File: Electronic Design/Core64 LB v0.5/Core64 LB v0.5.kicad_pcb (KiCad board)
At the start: 2 copper layers, 85 x 170 mm, 146 parts, among them IC1 TPS7A0533PDBVR, IC2 LP3961EMP-5.0, IC3 NCP176AMX330TCG, J1 HEADER_8-PIN_0.1, J10 TSM-106-03-T-DV‎, J11 SSW-116-22-F-S-VS‎, J12 TEENSY Cur. Mon., J13 Core Cur. Mon., J14 SSW-116-22-F-S-VS‎, J17 LED Cur. Mon., J2 HEADER_11-PIN_0.1, J3 Conn_01x08_Female, J4 PRG, J5 HEADER_8-PIN_0.1, J6 HEADER_8-PIN_0.1, J7 S03B-PASK-2_LF__SN_, J8 5V0 Cur. Mon., J9 3V3 Cur. Mon., Q1 MCC_SL3401A, Q10 MMBT4403LT1G, Q11 MMBT4403LT1G, Q12 MMBT4401LT1G, Q13 MMBT4403LT1G, Q14 MMBT4403LT1G, Q15 MMBT4401LT1G, Q16 MMBT4403LT1G, Q17 MMBT4403LT1G, Q18 MMBT4401LT1G, Q19 MMBT4401LT1G, Q2 MMBT4403LT1G, Q20 MMBT4401LT1G, Q21 MMBT4401LT1G, Q22 Q_NMOS_DGS_NVTR4503NT1G, Q3 MMBT4403LT1G, Q4 MMBT4403LT1G, Q5 MMBT4403LT1G, Q6 MMBT4401LT1G, Q7 MMBT4401LT1G, Q8 MMBT4401LT1G, Q9 MMBT4401LT1G, SW1 JS102011SAQN, U1 74HC02, U2 Teensy3.2, U3 SN74LV1T125DBVR, U4 M24C01-RMN, U5 74HC238, U6 Micro_LiPo_Charger, U7 LM393, U8 Adafruit_3.2_TFT_1743, X1 QWIIC, X2 Header_9-PIN_0.1, X3 SAO_conn_SFH11-NBPC-D03-ST-BK, X4 SSW-104-22-L-S-VS

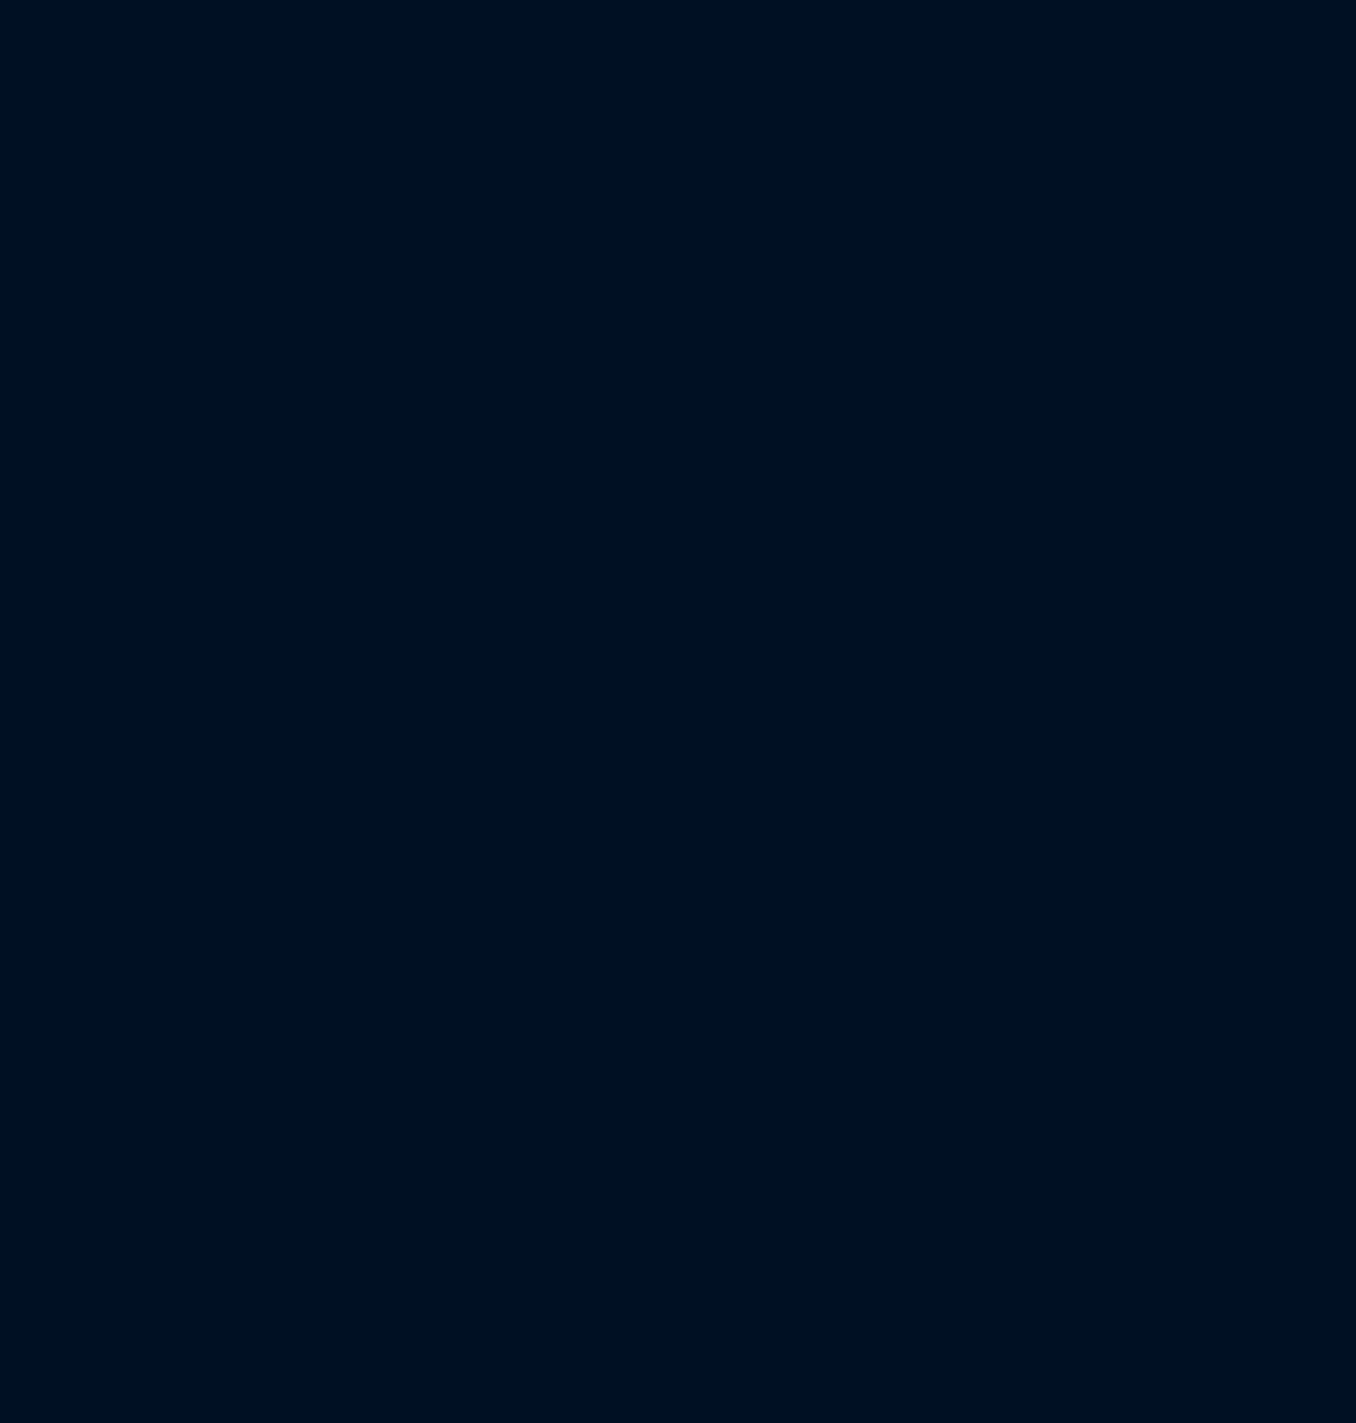
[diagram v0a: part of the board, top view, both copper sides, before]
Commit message: Update CB to be compatible with LM V0.1
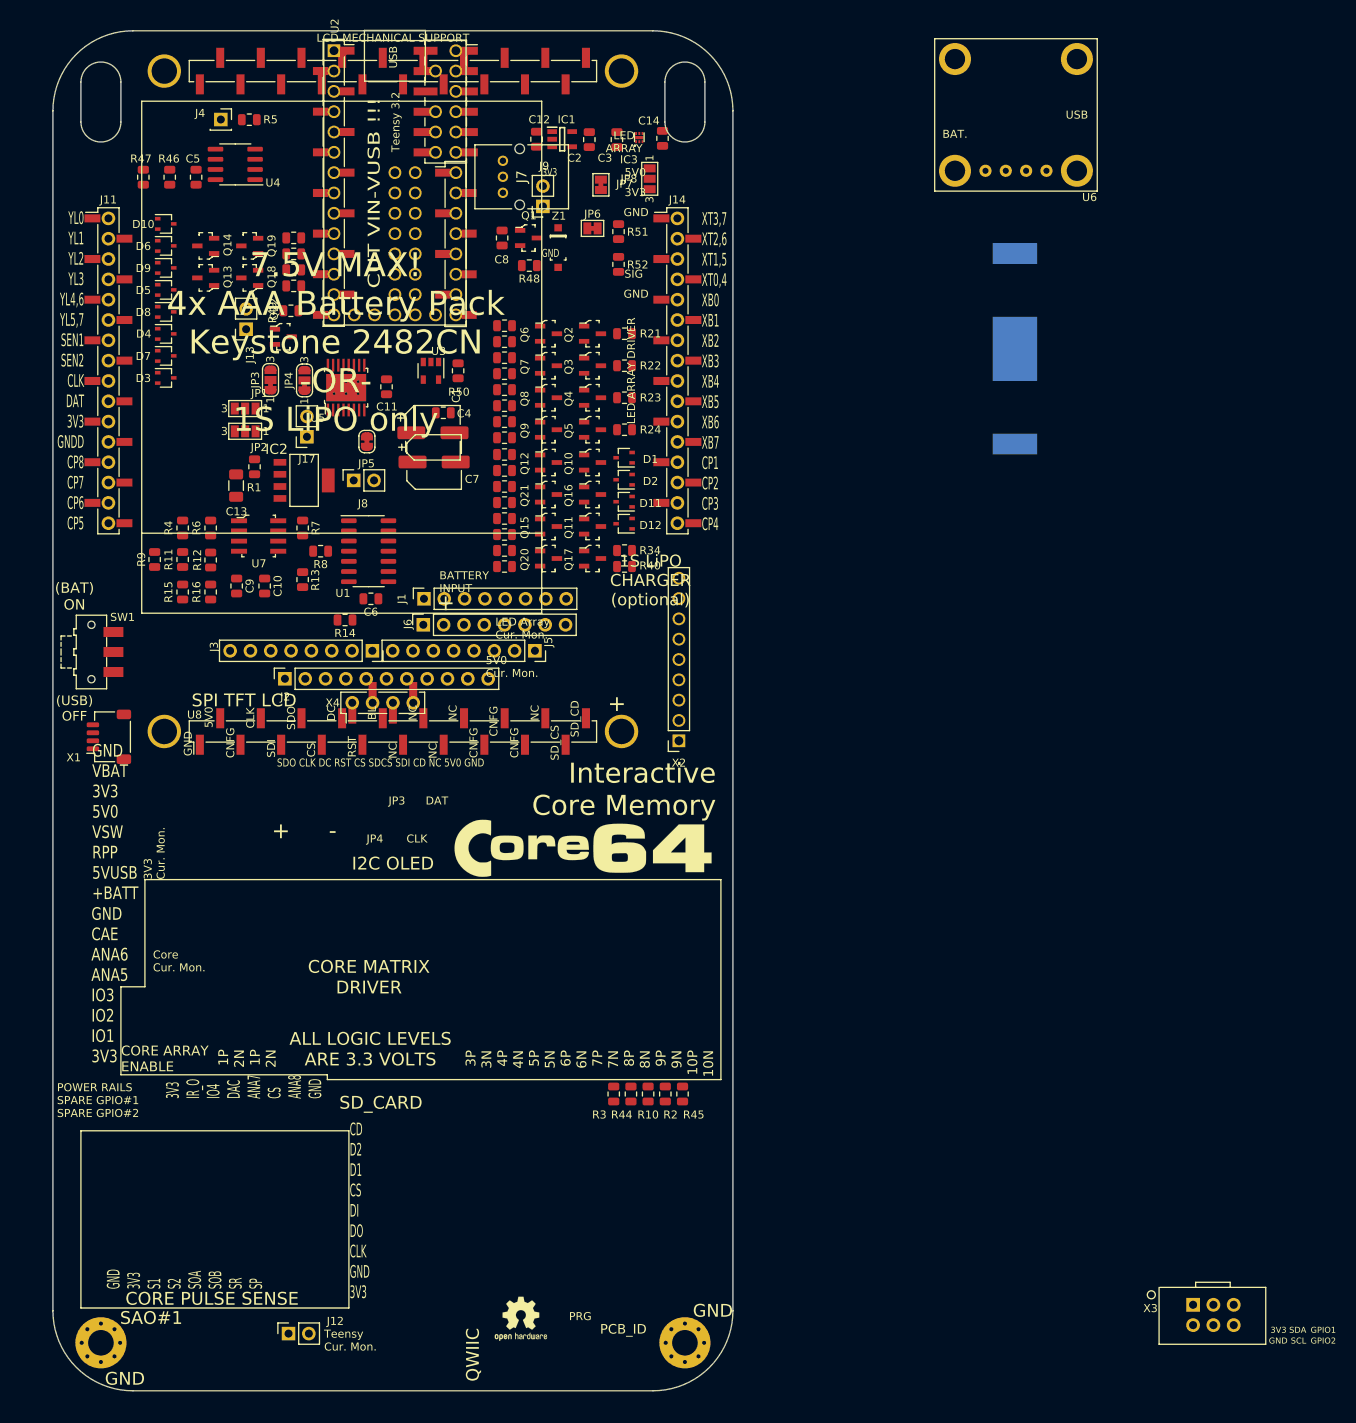
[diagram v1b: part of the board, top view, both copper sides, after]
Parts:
- added BT1: 3V, Battery:BatteryHolder_MPD_BC2003_1x2032, B.Cu at (229.2, -4.50)
- added C1: 470uF, Capacitor_SMD:CP_Elec_6.3x7.7, F.Cu at (156.5, 6.00)
- added C10: 10uF, Capacitor_SMD:C_0805_2012Metric, F.Cu at (135.5, 25.1)
- added C11: 0.1uF, Capacitor_SMD:C_0805_2012Metric, F.Cu at (150.7, 0.25)
- added C12: 1uF, Capacitor_SMD:C_0805_2012Metric, F.Cu at (169.4, -30.7)
- added C13: 68uF, Capacitor_SMD:C_1206_3216Metric, F.Cu at (131.9, 12.6)
- added C14: 1uF, Capacitor_SMD:C_0805_2012Metric, F.Cu at (185.2, -30.8)
- added C2: 1uF, Capacitor_SMD:C_0805_2012Metric, F.Cu at (176.1, -30.6)
- added C3: 1uF, Capacitor_SMD:C_0805_2012Metric, F.Cu at (179.5, -30.6)
- added C4: 0.1uF, Capacitor_SMD:C_0805_2012Metric, F.Cu at (157.8, 3.50)
- added C5: 0.1uF, Capacitor_SMD:C_0805_2012Metric, F.Cu at (126.9, -25.9)
- added C6: 0.1uF, Capacitor_SMD:C_0805_2012Metric, F.Cu at (148.8, 26.8)
- added C7: 470uF, Capacitor_SMD:CP_Elec_6.3x7.7, F.Cu at (156.7, 9.65)
- added C8: 0.01uF, Capacitor_SMD:C_0805_2012Metric, F.Cu at (165.2, -18.4)
- added C9: 0.1uF, Capacitor_SMD:C_0805_2012Metric, F.Cu at (132.0, 25.1)
- added D1: BAT54AW, Package_TO_SOT_SMD:SOT-323_SC-70, F.Cu at (180.4, 9.12)
- added D10: BAT54CW, Package_TO_SOT_SMD:SOT-323_SC-70, F.Cu at (123.1, -20.1)
- added D11: BAT54AW, Package_TO_SOT_SMD:SOT-323_SC-70, F.Cu at (180.4, 14.6)
- added D12: BAT54CW, Package_TO_SOT_SMD:SOT-323_SC-70, F.Cu at (180.4, 17.4)
- added D2: BAT54CW, Package_TO_SOT_SMD:SOT-323_SC-70, F.Cu at (180.4, 11.9)
- added D3: BAT54AW, Package_TO_SOT_SMD:SOT-323_SC-70, F.Cu at (123.1, -0.86)
- added D4: BAT54AW, Package_TO_SOT_SMD:SOT-323_SC-70, F.Cu at (123.1, -6.37)
- added D5: BAT54AW, Package_TO_SOT_SMD:SOT-323_SC-70, F.Cu at (123.1, -11.9)
- added D6: BAT54AW, Package_TO_SOT_SMD:SOT-323_SC-70, F.Cu at (123.1, -17.4)
- added D7: BAT54CW, Package_TO_SOT_SMD:SOT-323_SC-70, F.Cu at (123.1, -3.62)
- added D8: BAT54CW, Package_TO_SOT_SMD:SOT-323_SC-70, F.Cu at (123.1, -9.12)
- added D9: BAT54CW, Package_TO_SOT_SMD:SOT-323_SC-70, F.Cu at (123.1, -14.6)
- added H1: GND PAD, MountingHole:MountingHole_3.2mm_M3_Pad_Via, F.Cu at (115.0, 119.8)
- added H2: GND PAD, MountingHole:MountingHole_3.2mm_M3_Pad_Via, F.Cu at (188.0, 119.8)
- added IC1: TPS7A0533PDBVR, TPS7A0533PDBVR:SOT95P280X145-5N, F.Cu at (172.7, -30.7)
- added IC2: LP3961EMP-5.0, LP3961EMP-5.0:SOT150P696X180-5N, F.Cu at (140.4, 11.9)
- added IC3: NCP176AMX330TCG, NCP176AMX330TCG:NCP176AMX330TCG, F.Cu at (182.3, -30.9)
- added J1: HEADER_8-PIN_0.1, Connector_PinSocket_2.54mm:PinSocket_1x08_P2.54mm_Vertical, F.Cu at (155.4, 26.8)
- added J11: SSW-116-22-F-S-VS‎, Connector_PinHeader_2.54mm:PinHeader_1x16_P2.54mm_Vertical_SMD_and_TH_Pin1Left, F.Cu at (115.9, -1.75)
- added J12: TEENSY Cur. Mon., Connector_PinSocket_2.54mm:PinSocket_1x02_P2.54mm_Vertical, F.Cu at (138.4, 118.6)
- added J13: Core Cur. Mon., Connector_PinSocket_2.54mm:PinSocket_1x02_P2.54mm_Vertical, F.Cu at (133.2, -6.95)
- added J14: SSW-116-22-F-S-VS‎, Connector_PinHeader_2.54mm:PinHeader_1x16_P2.54mm_Vertical_SMD_and_TH_Pin1Left, F.Cu at (187.1, -1.75)
- added J17: LED Cur. Mon., Connector_PinSocket_2.54mm:PinSocket_1x02_P2.54mm_Vertical, F.Cu at (140.8, 6.50)
- added J2: HEADER_11-PIN_0.1, Connector_PinSocket_2.54mm:PinSocket_1x11_P2.54mm_Vertical, F.Cu at (138.0, 36.8)
- added J3: Conn_01x08_Female, Connector_PinSocket_2.54mm:PinSocket_1x08_P2.54mm_Vertical, F.Cu at (148.9, 33.2)
- added J4: PRG, Connector_PinSocket_2.54mm:PinSocket_1x01_P2.54mm_Vertical, F.Cu at (130.0, -33.2)
- added J5: HEADER_8-PIN_0.1, Connector_PinSocket_2.54mm:PinSocket_1x08_P2.54mm_Vertical, F.Cu at (169.2, 33.2)
- added J6: HEADER_8-PIN_0.1, Connector_PinSocket_2.54mm:PinSocket_1x08_P2.54mm_Vertical, F.Cu at (155.3, 30.0)
- added J7: S03B-PASK-2_LF__SN_, JST_S03B-PASK-2_LF__SN_:S03BPASK2LFSN, F.Cu at (165.2, -24.0)
- added J8: 5V0 Cur. Mon., Connector_PinSocket_2.54mm:PinSocket_1x02_P2.54mm_Vertical, F.Cu at (146.6, 11.9)
- added J9: 3V3 Cur. Mon., Connector_PinSocket_2.54mm:PinSocket_1x02_P2.54mm_Vertical, F.Cu at (170.2, -22.3)
- added JP1: SolderJumper_3_Open, Jumper:SolderJumper-3_P1.3mm_Open_Pad1.0x1.5mm_NumberLabels, F.Cu at (133.0, 2.97)
- added JP2: SolderJumper_3_Open, Jumper:SolderJumper-3_P1.3mm_Open_Pad1.0x1.5mm_NumberLabels, F.Cu at (133.0, 5.81)
- added JP3: SolderJumper_3_Open, Jumper:SolderJumper-3_P1.3mm_Bridged12_RoundedPad1.0x1.5mm_NumberLabels, F.Cu at (136.2, -0.60)
- added JP4: SolderJumper_3_Open, Jumper:SolderJumper-3_P1.3mm_Bridged12_RoundedPad1.0x1.5mm_NumberLabels, F.Cu at (140.4, -0.55)
- added JP5: Teensy_Charge_Enable, Jumper:SolderJumper-2_P1.3mm_Bridged_RoundedPad1.0x1.5mm, F.Cu at (148.2, 7.10)
- added JP6: Opt. Cur. Mon., Jumper:SolderJumper-2_P1.3mm_Bridged_Pad1.0x1.5mm, F.Cu at (176.4, -19.6)
- added JP7: USB_Power_Enable, Jumper:SolderJumper-2_P1.3mm_Bridged_Pad1.0x1.5mm, F.Cu at (177.5, -25.0)
- added JP8: 3V3_Select, Jumper:SolderJumper-3_P1.3mm_Open_Pad1.0x1.5mm_NumberLabels, F.Cu at (183.6, -25.8)
- added L1: Core_64_Logo, Core_Memory_8x8_Array:Core64_Logo, F.Cu at (175.5, 58.2)
- added L2: Core_64_Logo, Core_Memory_8x8_Array:Core64_Logo, B.Cu at (151.5, -34.8)
- added L3: Core_64_MachineIdeas_Link, Core_Memory_8x8_Array:Core64_QR_Link_MachineIdeas, B.Cu at (151.5, -0.05)
- added L4: Logo_Open_Hardware_Small, Symbol:OSHW-Logo2_7.3x6mm_SilkScreen, F.Cu at (167.5, 116.8)
- added Q1: MCC_SL3401A, Digikey:SOT-23-3, F.Cu at (168.4, -18.4)
- added Q10: MMBT4403LT1G, Digikey:SOT-23-3, F.Cu at (176.4, 9.71)
- added Q11: MMBT4403LT1G, Digikey:SOT-23-3, F.Cu at (176.4, 17.7)
- added Q12: MMBT4401LT1G, Digikey:SOT-23-3, F.Cu at (170.9, 9.71)
- added Q13: MMBT4403LT1G, Digikey:SOT-23-3, F.Cu at (128.1, -13.4)
- added Q14: MMBT4403LT1G, Digikey:SOT-23-3, F.Cu at (128.1, -17.4)
- added Q15: MMBT4401LT1G, Digikey:SOT-23-3, F.Cu at (170.9, 17.7)
- added Q16: MMBT4403LT1G, Digikey:SOT-23-3, F.Cu at (176.4, 13.7)
- added Q17: MMBT4403LT1G, Digikey:SOT-23-3, F.Cu at (176.4, 21.7)
- added Q18: MMBT4401LT1G, Digikey:SOT-23-3, F.Cu at (133.6, -13.4)
- added Q19: MMBT4401LT1G, Digikey:SOT-23-3, F.Cu at (133.6, -17.4)
- added Q2: MMBT4403LT1G, Digikey:SOT-23-3, F.Cu at (176.4, -6.38)
- added Q20: MMBT4401LT1G, Digikey:SOT-23-3, F.Cu at (170.9, 21.7)
- added Q21: MMBT4401LT1G, Digikey:SOT-23-3, F.Cu at (170.9, 13.7)
- added Q22: Q_NMOS_DGS_NVTR4503NT1G, Digikey:SOT-23-3, F.Cu at (137.8, -6.00)
- added Q3: MMBT4403LT1G, Digikey:SOT-23-3, F.Cu at (176.4, -2.38)
- added Q4: MMBT4403LT1G, Digikey:SOT-23-3, F.Cu at (176.4, 1.61)
- added Q5: MMBT4403LT1G, Digikey:SOT-23-3, F.Cu at (176.4, 5.62)
- added Q6: MMBT4401LT1G, Digikey:SOT-23-3, F.Cu at (170.9, -6.38)
- added Q7: MMBT4401LT1G, Digikey:SOT-23-3, F.Cu at (170.9, -2.38)
- added Q8: MMBT4401LT1G, Digikey:SOT-23-3, F.Cu at (170.9, 1.61)
- added Q9: MMBT4401LT1G, Digikey:SOT-23-3, F.Cu at (170.9, 5.62)
- added R1: 10k, Resistor_SMD:R_0805_2012Metric, F.Cu at (134.2, 10.2)
- added R10: 10k, Resistor_SMD:R_0805_2012Metric, F.Cu at (183.4, 88.7)
- added R11: 11-1%, Resistor_SMD:R_0805_2012Metric, F.Cu at (125.2, 21.8)
- added R12: 11-1%, Resistor_SMD:R_0805_2012Metric, F.Cu at (128.7, 21.9)
- added R13: 10k, Resistor_SMD:R_0805_2012Metric, F.Cu at (140.2, 24.4)
- added R14: 10k, Resistor_SMD:R_0805_2012Metric, F.Cu at (145.5, 29.4)
- added R15: 1K5-1%, Resistor_SMD:R_0805_2012Metric, F.Cu at (125.2, 25.9)
- added R16: 1K5-1%, Resistor_SMD:R_0805_2012Metric, F.Cu at (128.7, 25.9)
- added R17: 470, Resistor_SMD:R_0805_2012Metric, F.Cu at (165.4, -7.38)
- added R18: 470, Resistor_SMD:R_0805_2012Metric, F.Cu at (165.4, -3.38)
- added R19: 470, Resistor_SMD:R_0805_2012Metric, F.Cu at (165.4, 0.61)
- added R2: 10k, Resistor_SMD:R_0805_2012Metric, F.Cu at (185.6, 88.7)
- added R20: 470, Resistor_SMD:R_0805_2012Metric, F.Cu at (165.4, 4.62)
- added R21: 6R8-1%, Resistor_SMD:R_0805_2012Metric, F.Cu at (180.4, -6.38)
- added R22: 6R8-1%, Resistor_SMD:R_0805_2012Metric, F.Cu at (180.4, -2.38)
- added R23: 6R8-1%, Resistor_SMD:R_0805_2012Metric, F.Cu at (180.4, 1.61)
- added R24: 6R8-1%, Resistor_SMD:R_0805_2012Metric, F.Cu at (180.4, 5.62)
- added R25: 470, Resistor_SMD:R_0805_2012Metric, F.Cu at (165.4, -5.38)
- added R26: 470, Resistor_SMD:R_0805_2012Metric, F.Cu at (165.4, -1.39)
- added R27: 470, Resistor_SMD:R_0805_2012Metric, F.Cu at (165.4, 2.62)
- added R28: 470, Resistor_SMD:R_0805_2012Metric, F.Cu at (165.4, 6.62)
- added R29: 470, Resistor_SMD:R_0805_2012Metric, F.Cu at (165.4, 8.71)
- added R3: 10k, Resistor_SMD:R_0805_2012Metric, F.Cu at (179.1, 88.7)
- added R30: 470, Resistor_SMD:R_0805_2012Metric, F.Cu at (165.4, 16.7)
- added R31: 470, Resistor_SMD:R_0805_2012Metric, F.Cu at (165.4, 10.7)
- added R32: 470, Resistor_SMD:R_0805_2012Metric, F.Cu at (139.1, -12.4)
- added R33: 470, Resistor_SMD:R_0805_2012Metric, F.Cu at (139.1, -16.4)
- added R34: 6R8-1%, Resistor_SMD:R_0805_2012Metric, F.Cu at (180.4, 20.7)
- added R35: 470, Resistor_SMD:R_0805_2012Metric, F.Cu at (165.4, 18.7)
- added R36: 470, Resistor_SMD:R_0805_2012Metric, F.Cu at (165.4, 12.7)
- added R37: 470, Resistor_SMD:R_0805_2012Metric, F.Cu at (165.4, 20.7)
- added R38: 470, Resistor_SMD:R_0805_2012Metric, F.Cu at (139.1, -14.4)
- added R39: 470, Resistor_SMD:R_0805_2012Metric, F.Cu at (139.1, -18.4)
- added R4: 1K8-1%, Resistor_SMD:R_0805_2012Metric, F.Cu at (125.2, 17.9)
- added R40: 6R8-1%, Resistor_SMD:R_0805_2012Metric, F.Cu at (180.4, 22.7)
- added R41: 470, Resistor_SMD:R_0805_2012Metric, F.Cu at (165.4, 22.7)
- added R42: 470, Resistor_SMD:R_0805_2012Metric, F.Cu at (165.4, 14.7)
- added R44: 10k, Resistor_SMD:R_0805_2012Metric, F.Cu at (181.2, 88.7)
- added R45: 10k, Resistor_SMD:R_0805_2012Metric, F.Cu at (187.7, 88.7)
- added R46: 2K2, Resistor_SMD:R_0805_2012Metric, F.Cu at (123.6, -25.9)
- added R47: 2K2, Resistor_SMD:R_0805_2012Metric, F.Cu at (120.3, -25.9)
- added R48: 10k, Resistor_SMD:R_0805_2012Metric, F.Cu at (168.6, -14.9)
- added R49: 10k, Resistor_SMD:R_0805_2012Metric, F.Cu at (138.8, -9.25)
- added R5: 10k, Resistor_SMD:R_0805_2012Metric, F.Cu at (133.6, -33.1)
- added R50: 470, Resistor_SMD:R_0805_2012Metric, F.Cu at (159.7, -1.75)
- added R51: 33k, Resistor_SMD:R_0805_2012Metric, F.Cu at (179.7, -19.1)
- added R52: 11k, Resistor_SMD:R_0805_2012Metric, F.Cu at (179.7, -15.1)
- added R6: 1K8-1%, Resistor_SMD:R_0805_2012Metric, F.Cu at (128.7, 17.9)
- added R7: 10k, Resistor_SMD:R_0805_2012Metric, F.Cu at (140.2, 17.9)
- added R8: 10k, Resistor_SMD:R_0805_2012Metric, F.Cu at (142.5, 20.8)
- added R9: 1K5-1%, Resistor_SMD:R_0805_2012Metric, F.Cu at (121.7, 21.8)
- added SW1: JS102011SAQN, Button_Switch_SMD:SW_SPDT_CK-JS102011SAQN, F.Cu at (113.8, 33.4)
- added U1: 74HC02, Package_SO:SOIC-14_3.9x8.7mm_P1.27mm, F.Cu at (148.5, 20.8)
- added U2: Teensy3.2, Teensy:Teensy30_31_32_LC_SMD_SOCKETS, F.Cu at (151.8, -25.2)
- added U3: SN74LV1T125DBVR, Package_TO_SOT_SMD:SOT-23-5, F.Cu at (156.2, -1.75)
- added U4: M24C01-RMN, Package_SO:SOIC-8_3.9x4.9mm_P1.27mm, F.Cu at (131.8, -27.6)
- added U5: 74HC238, Digikey:TSSOP-16-1EP_W4.40mm, F.Cu at (145.7, 0.35)
- added U6: Micro_LiPo_Charger, Core_Memory_8x8_Array:Micro_LiPo_Charger, F.Cu at (229.4, -33.7)
- added U7: LM393, Digikey:SOIC-8_W3.9mm, F.Cu at (134.7, 18.9)
- added U8: Adafruit_3.2_TFT_1743, Adafruit_3.2_TFT:Adafruit_3.2_TFT_Dual_PinHeader_1x20_P2.54mm_Vertical_SMD_Pin1Left, F.Cu at (151.5, 43.3)
- added X1: QWIIC, Connector_JST:JST_SH_SM04B-SRSS-TB_1x04-1MP_P1.00mm_Horizontal, F.Cu at (116.0, 44.0)
- added X2: Header_9-PIN_0.1, Connector_PinSocket_2.54mm:PinSocket_1x09_P2.54mm_Vertical, F.Cu at (187.2, 44.5)
- added X3: SAO_conn_SFH11-NBPC-D03-ST-BK, badgelife_sao_v169bis:Badgelife-SAOv169-BADGE-2x3, F.Cu at (254.0, 116.2)
- added X4: SSW-104-22-L-S-VS, Connector_PinSocket_2.54mm:PinSocket_1x04_P2.54mm_Vertical_SMD_and_TH_Pin1Left, F.Cu at (150.2, 39.8)
- added Z1: PDZ10BGWX_(10V), Digikey:SOD-123, F.Cu at (172.2, -17.1)
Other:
- board size 85 x 170 mm -> 236.5 x 171.8 mm

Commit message: Update 16p to 20p headers for CB
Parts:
- removed the BT1 at (229.2, -4.50)
- removed the C1 at (156.5, 6.00)
- removed the C10 at (135.5, 25.1)
- removed the C11 at (150.7, 0.25)
- removed the C12 at (169.4, -30.7)
- removed the C13 at (131.9, 12.6)
- removed the C14 at (185.2, -30.8)
- removed the C2 at (176.1, -30.6)
- removed the C3 at (179.5, -30.6)
- removed the C4 at (157.8, 3.50)
- removed the C5 at (126.9, -25.9)
- removed the C6 at (148.8, 26.8)
- removed the C7 at (156.7, 9.65)
- removed the C8 at (165.2, -18.4)
- removed the C9 at (132.0, 25.1)
- removed the D1 at (180.4, 9.12)
- removed the D10 at (123.1, -20.1)
- removed the D11 at (180.4, 14.6)
- removed the D12 at (180.4, 17.4)
- removed the D2 at (180.4, 11.9)
- removed the D3 at (123.1, -0.86)
- removed the D4 at (123.1, -6.37)
- removed the D5 at (123.1, -11.9)
- removed the D6 at (123.1, -17.4)
- removed the D7 at (123.1, -3.62)
- removed the D8 at (123.1, -9.12)
- removed the D9 at (123.1, -14.6)
- removed the H1 at (115.0, 119.8)
- removed the H2 at (188.0, 119.8)
- removed the IC1 at (172.7, -30.7)
- removed the IC2 at (140.4, 11.9)
- removed the IC3 at (182.3, -30.9)
- removed the J1 at (155.4, 26.8)
- removed the J11 at (115.9, -1.75)
- removed the J11 at (-35.6, 0.00)
- removed the J12 at (138.4, 118.6)
- removed the J13 at (133.2, -6.95)
- removed the J14 at (187.1, -1.75)
- removed the J14 at (35.6, 0.00)
- removed the J17 at (140.8, 6.50)
- removed the J2 at (138.0, 36.8)
- removed the J3 at (148.9, 33.2)
- removed the J4 at (130.0, -33.2)
- removed the J5 at (169.2, 33.2)
- removed the J6 at (155.3, 30.0)
- removed the J7 at (165.2, -24.0)
- removed the J8 at (146.6, 11.9)
- removed the J9 at (170.2, -22.3)
- removed the JP1 at (133.0, 2.97)
- removed the JP2 at (133.0, 5.81)
- removed the JP3 at (136.2, -0.60)
- removed the JP4 at (140.4, -0.55)
- removed the JP5 at (148.2, 7.10)
- removed the JP6 at (176.4, -19.6)
- removed the JP7 at (177.5, -25.0)
- removed the JP8 at (183.6, -25.8)
- removed the L1 at (175.5, 58.2)
- removed the L2 at (151.5, -34.8)
- removed the L3 at (151.5, -0.05)
- removed the L4 at (167.5, 116.8)
- removed the Q1 at (168.4, -18.4)
- removed the Q10 at (176.4, 9.71)
- removed the Q11 at (176.4, 17.7)
- removed the Q12 at (170.9, 9.71)
- removed the Q13 at (128.1, -13.4)
- removed the Q14 at (128.1, -17.4)
- removed the Q15 at (170.9, 17.7)
- removed the Q16 at (176.4, 13.7)
- removed the Q17 at (176.4, 21.7)
- removed the Q18 at (133.6, -13.4)
- removed the Q19 at (133.6, -17.4)
- removed the Q2 at (176.4, -6.38)
- removed the Q20 at (170.9, 21.7)
- removed the Q21 at (170.9, 13.7)
- removed the Q22 at (137.8, -6.00)
- removed the Q3 at (176.4, -2.38)
- removed the Q4 at (176.4, 1.61)
- removed the Q5 at (176.4, 5.62)
- removed the Q6 at (170.9, -6.38)
- removed the Q7 at (170.9, -2.38)
- removed the Q8 at (170.9, 1.61)
- removed the Q9 at (170.9, 5.62)
- removed the R1 at (134.2, 10.2)
- removed the R10 at (183.4, 88.7)
- removed the R11 at (125.2, 21.8)
- removed the R12 at (128.7, 21.9)
- removed the R13 at (140.2, 24.4)
- removed the R14 at (145.5, 29.4)
- removed the R15 at (125.2, 25.9)
- removed the R16 at (128.7, 25.9)
- removed the R17 at (165.4, -7.38)
- removed the R18 at (165.4, -3.38)
- removed the R19 at (165.4, 0.61)
- removed the R2 at (185.6, 88.7)
- removed the R20 at (165.4, 4.62)
- removed the R21 at (180.4, -6.38)
- removed the R22 at (180.4, -2.38)
- removed the R23 at (180.4, 1.61)
- removed the R24 at (180.4, 5.62)
- removed the R25 at (165.4, -5.38)
- removed the R26 at (165.4, -1.39)
- removed the R27 at (165.4, 2.62)
- removed the R28 at (165.4, 6.62)
- removed the R29 at (165.4, 8.71)
- removed the R3 at (179.1, 88.7)
- removed the R30 at (165.4, 16.7)
- removed the R31 at (165.4, 10.7)
- removed the R32 at (139.1, -12.4)
- removed the R33 at (139.1, -16.4)
- removed the R34 at (180.4, 20.7)
- removed the R35 at (165.4, 18.7)
- removed the R36 at (165.4, 12.7)
- removed the R37 at (165.4, 20.7)
- removed the R38 at (139.1, -14.4)
- removed the R39 at (139.1, -18.4)
- removed the R4 at (125.2, 17.9)
- removed the R40 at (180.4, 22.7)
- removed the R41 at (165.4, 22.7)
- removed the R42 at (165.4, 14.7)
- removed the R44 at (181.2, 88.7)
- removed the R45 at (187.7, 88.7)
- removed the R46 at (123.6, -25.9)
- removed the R47 at (120.3, -25.9)
- removed the R48 at (168.6, -14.9)
- removed the R49 at (138.8, -9.25)
- removed the R5 at (133.6, -33.1)
- removed the R50 at (159.7, -1.75)
- removed the R51 at (179.7, -19.1)
- removed the R52 at (179.7, -15.1)
- removed the R6 at (128.7, 17.9)
- removed the R7 at (140.2, 17.9)
- removed the R8 at (142.5, 20.8)
- removed the R9 at (121.7, 21.8)
- removed the SW1 at (113.8, 33.4)
- removed the U1 at (148.5, 20.8)
- removed the U2 at (151.8, -25.2)
- removed the U3 at (156.2, -1.75)
- removed the U4 at (131.8, -27.6)
- removed the U5 at (145.7, 0.35)
- removed the U6 at (229.4, -33.7)
- removed the U7 at (134.7, 18.9)
- removed the U8 at (151.5, 43.3)
- removed the X1 at (116.0, 44.0)
- removed the X2 at (187.2, 44.5)
- removed the X3 at (254.0, 116.2)
- removed the X4 at (150.2, 39.8)
- removed the Z1 at (172.2, -17.1)
- added J11: SSW-116-22-F-S-VS‎, Connector_PinHeader_2.54mm:PinHeader_1x20_P2.54mm_Vertical, F.Cu at (-35.6, -24.1)
- added J14: SSW-116-22-F-S-VS‎, Connector_PinHeader_2.54mm:PinHeader_1x20_P2.54mm_Vertical, F.Cu at (35.6, -24.1)
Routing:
- net -BATT: track 896.6 -> 903.2 mm
- net 5V0: track 354.7 -> 360.8 mm, vias 14 -> 15
- net I2C_CLOCK: track 234.8 -> 231.1 mm
- net YL4: track 136.6 -> 134.6 mm
- net YL2: track 140.9 -> 138.9 mm
- net YL0: track 142.8 -> 140.8 mm
- net CP8_EN: track 46.2 -> 44.2 mm
- net CP6_EN: track 30.7 -> 28.7 mm
- net CP4_EN: track 58.5 -> 56.5 mm
- net CP2_EN: track 70.3 -> 68.3 mm
- net XT0,4: track 158.5 -> 160.2 mm
- net I2C_DATA: track 234.3 -> 232.7 mm
- net SENSE2: track 130.5 -> 128.9 mm
- net XB7: track 105.2 -> 103.6 mm
- net XB5: track 111.4 -> 109.8 mm
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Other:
- board size 236.5 x 171.8 mm -> 85 x 170 mm
